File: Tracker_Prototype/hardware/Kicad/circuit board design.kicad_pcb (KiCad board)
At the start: 2 copper layers, 35.6 x 26.4 mm, 8 parts, among them U1 MAX-M8C, U3 CMWX1ZZABZ-078, U6 MS5607-02BA

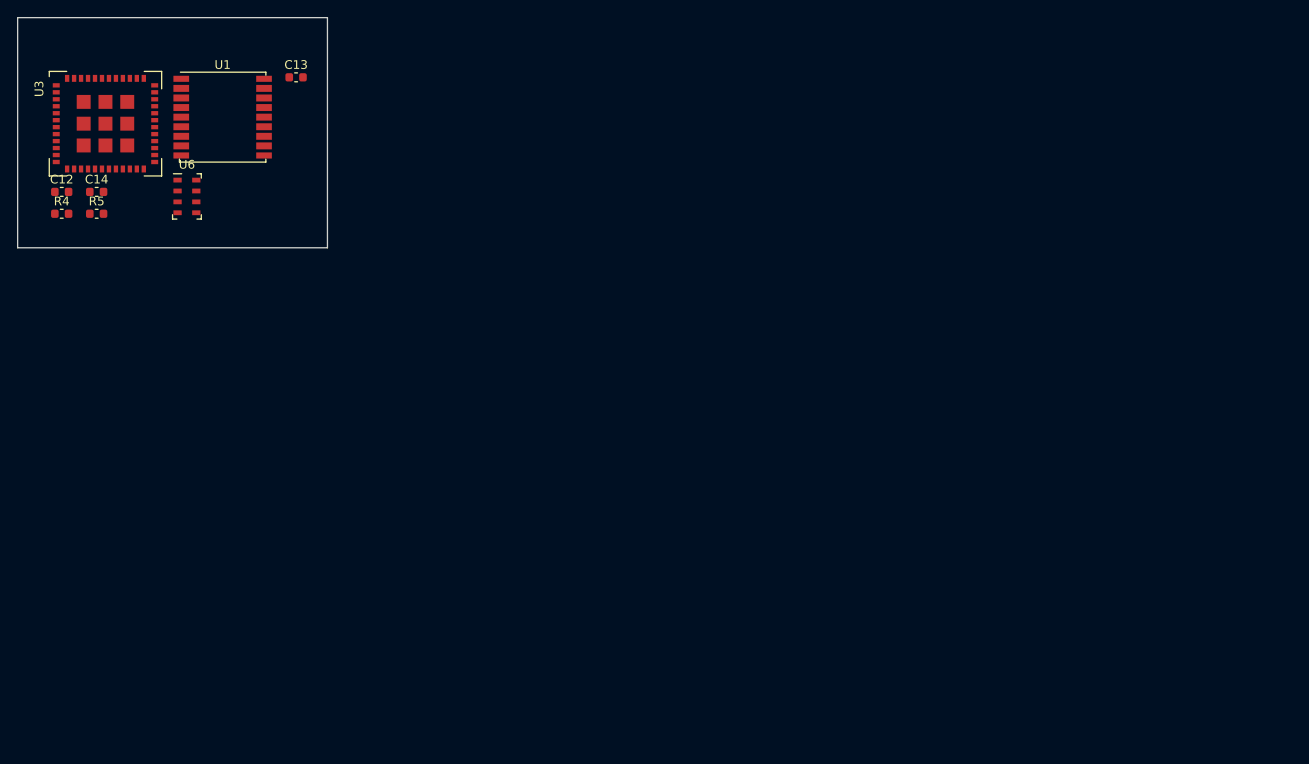
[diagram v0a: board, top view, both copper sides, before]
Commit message: made some edits to the circuit to remove ERC errors. Added in footprints from Femto
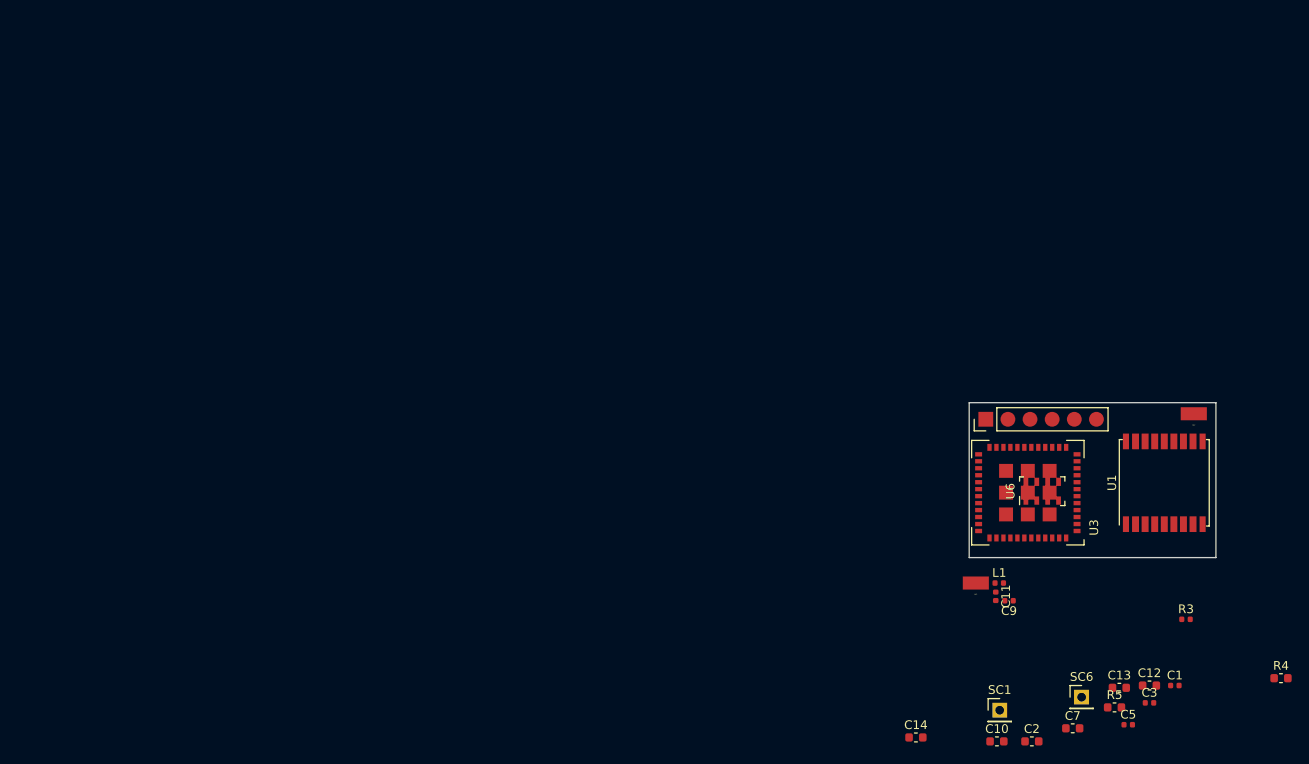
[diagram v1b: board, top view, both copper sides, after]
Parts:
- added AE1: Lora Antenna, femto_footprints:PAD_3x1.5, F.Cu at (267.5, 180.7)
- added AE2: GPS Antenna, femto_footprints:PAD_3x1.5, F.Cu at (292.5, 161.3)
- added C1: 100nF, Capacitor_SMD:C_0402_1005Metric, F.Cu at (290.3, 192.5)
- added C10: 10uF, Capacitor_SMD:C_0603_1608Metric, F.Cu at (269.9, 198.9)
- added C11: NF, Capacitor_SMD:C_0402_1005Metric, F.Cu at (269.7, 182.2)
- added C2: 10uF, Capacitor_SMD:C_0603_1608Metric, F.Cu at (273.9, 198.9)
- added C3: 100nF, Capacitor_SMD:C_0402_1005Metric, F.Cu at (287.4, 194.5)
- added C5: 100nF, Capacitor_SMD:C_0402_1005Metric, F.Cu at (285.0, 197.0)
- added C7: 1uF, Capacitor_SMD:C_0603_1608Metric, F.Cu at (278.6, 197.4)
- added C9: NF, Capacitor_SMD:C_0402_1005Metric, F.Cu at (271.3, 182.8)
- added J1: Conn_01x06, femto_footprints:special_test_pads, F.Cu at (268.6, 161.9)
- added L1: NF, Capacitor_SMD:C_0402_1005Metric, F.Cu at (270.2, 180.7)
- added R3: 10K, Resistor_SMD:R_0402_1005Metric, F.Cu at (291.6, 184.9)
- added SC1: Solar_Cell, Connector_PinHeader_2.54mm:PinHeader_1x01_P2.54mm_Vertical, F.Cu at (270.2, 195.3)
- added SC6: Solar_Cell, Connector_PinHeader_2.54mm:PinHeader_1x01_P2.54mm_Vertical, F.Cu at (279.6, 193.8)
- moved R4 149.8 mm to (302.5, 191.6)
- moved C12 137.1 mm to (287.4, 192.5)
- moved R5 129.8 mm to (283.4, 195.0)
- moved C13 117.6 mm to (283.9, 192.7)
- moved U1 115.9 mm to (289.1, 169.2), turned to 90 degrees
- moved U3 114.0 mm to (273.4, 170.3), turned to 180 degrees
- moved C14 113.0 mm to (260.6, 198.4)
- moved U6 103.8 mm to (275.1, 170.2), turned to 90 degrees
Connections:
- U1 pad 13: Net-(U1-Pad13) -> (no net)
- U1 pad 14: Net-(U1-Pad14) -> (no net)
- U1 pad 15: Net-(U1-Pad15) -> (no net)
- U1 pad 2: Net-(U1-Pad2) -> (no net)
- U1 pad 3: Net-(U1-Pad3) -> (no net)
- U3 pad 1: Net-(U3-Pad1) -> (no net)
- U3 pad 10: Net-(U3-Pad10) -> (no net)
- U3 pad 11: Net-(U3-Pad11) -> (no net)
- U3 pad 12: Net-(U3-Pad12) -> (no net)
- U3 pad 13: Net-(U3-Pad13) -> (no net)
- U3 pad 18: Net-(U3-Pad18) -> (no net)
- U3 pad 19: Net-(U3-Pad19) -> (no net)
- U3 pad 2: Net-(U3-Pad2) -> (no net)
- U3 pad 20: Net-(U3-Pad20) -> (no net)
- U3 pad 21: Net-(U3-Pad21) -> (no net)
- U3 pad 22: Net-(U3-Pad22) -> (no net)
- U3 pad 23: Net-(U3-Pad23) -> (no net)
- U3 pad 24: Net-(U3-Pad24) -> (no net)
- U3 pad 28: Net-(U3-Pad28) -> (no net)
- U3 pad 29: Net-(U3-Pad29) -> (no net)
- U3 pad 30: Net-(U3-Pad30) -> (no net)
- U3 pad 31: Net-(U3-Pad31) -> (no net)
- U3 pad 32: Net-(U3-Pad32) -> (no net)
- U3 pad 33: Net-(U3-Pad33) -> (no net)
- U3 pad 37: Net-(U3-Pad37) -> (no net)
- U3 pad 38: Net-(U3-Pad38) -> (no net)
- U3 pad 39: Net-(U3-Pad39) -> (no net)
- U3 pad 40: Net-(U3-Pad40) -> (no net)
- U3 pad 45: Net-(U3-Pad45) -> (no net)
- U3 pad 46: Net-(U3-Pad46) -> (no net)
- U3 pad 47: Net-(U3-Pad47) -> (no net)
- U3 pad 8: Net-(U3-Pad8) -> (no net)
- U3 pad 9: Net-(U3-Pad9) -> (no net)
- U6 pad 6: Net-(U6-Pad6) -> (no net)
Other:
- board size 35.6 x 26.4 mm -> 28.3 x 17.8 mm

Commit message: changed the footprints for GPS antenna and lora antenna
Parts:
- removed SC1, SC6: Solar_Cell, Connector_PinHeader_2.54mm:PinHeader_1x01_P2.54mm_Vertical
- added J2: Conn_01x01, Connector_PinHeader_1.00mm:PinHeader_1x01_P1.00mm_Vertical, F.Cu at (298.3, 166.1)
- added J3: Conn_01x01, Connector_PinHeader_1.00mm:PinHeader_1x01_P1.00mm_Vertical, F.Cu at (298.3, 169.5)
- AE1, AE2: footprint femto_footprints:PAD_3x1.5 -> Connector_PinHeader_1.00mm:PinHeader_1x01_P1.00mm_Vertical
- C12: footprint Capacitor_SMD:C_0603_1608Metric -> Capacitor_SMD:C_0402_1005Metric
- J1, U6: moved to B.Cu
- R4, R5: footprint Resistor_SMD:R_0603_1608Metric -> Resistor_SMD:R_0402_1005Metric
- moved AE1 19.6 mm to (269.0, 161.2)
- moved C11 19.6 mm to (271.3, 162.7)
- moved C9 19.6 mm to (272.8, 163.2)
- moved L1 19.6 mm to (271.7, 161.2)
- moved J1 14.1 mm to (268.7, 176.0), turned to 270 degrees
- moved U3 1.95 mm to (275.4, 170.3), turned to 90 degrees
- turned U6 to 270 degrees
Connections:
- U1 pad 13: (no net) -> GND
- U3 pad 14: /GPS_TIMEPULSE -> /VDD_TCXO
- U3 pad 15: /VDD_TCXO -> /GPS_TIMEPULSE
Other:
- board size 28.3 x 17.8 mm -> 30.9 x 17.8 mm
